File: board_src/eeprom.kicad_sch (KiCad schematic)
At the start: 5 parts, among them IC2 M24C02-WMN6TP, J6 Conn_01x02_Pin, J8 Conn_01x01_Pin

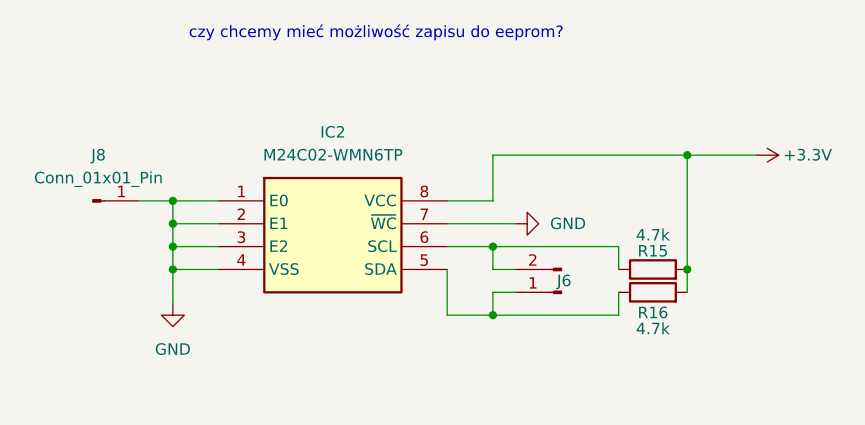
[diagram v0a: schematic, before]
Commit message: Wersja ze sciezkami miedzianymi
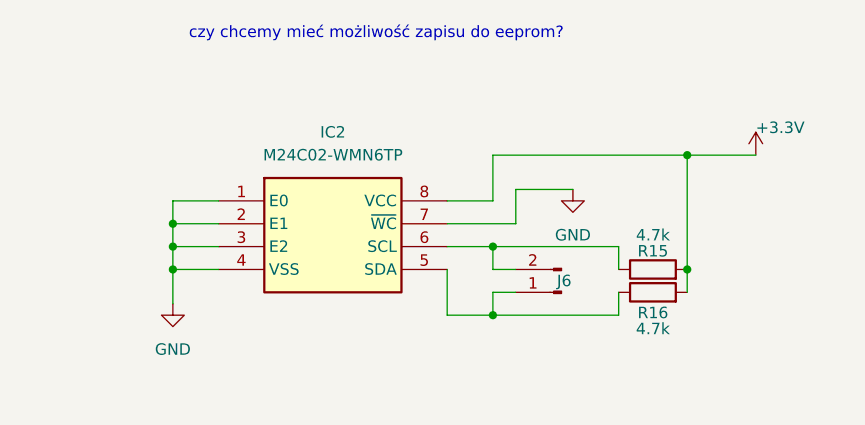
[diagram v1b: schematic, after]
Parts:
- removed J8: Conn_01x01_Pin, Connector_PinHeader_2.54mm:PinHeader_1x01_P2.54mm_Vertical, symbol Connector:Conn_01x01_Pin
- R15, R16: footprint Resistor_SMD:R_1206_3216Metric -> Resistor_SMD:R_0603_1608Metric
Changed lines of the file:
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@@
-	)
-	(junction
-		(at 149.86 90.17)
-		(diameter 0)
-		(color 0 0 0 0)
 	)
 	(junction
@@
 	(wire
 		(pts
-			(xy 146.05 90.17) (xy 149.86 90.17)
+			(xy 187.96 92.71) (xy 180.34 92.71)
 		)
 		(stroke
@@
 	(wire
 		(pts
-			(xy 180.34 92.71) (xy 187.96 92.71)
+			(xy 187.96 88.9) (xy 194.31 88.9)
 		)
 		(stroke
@@
 	(wire
 		(pts
+			(xy 187.96 88.9) (xy 187.96 92.71)
+		)
+		(stroke
+			(width 0)
+			(type default)
+		)
+	)
+	(wire
+		(pts
 			(xy 149.86 90.17) (xy 149.86 92.71)
 		)
@@
 			(width 0)
 			(type default)
-		)
-	)
-	(symbol
-		(lib_id "Connector:Conn_01x01_Pin")
-		(at 140.97 90.17 0)
-		(unit 1)
-		(exclude_from_sim no)
-		(in_bom yes)
-		(on_board yes)
-		(dnp no)
-		(fields_autoplaced yes)
-		(property "Reference" "J8"
-			(at 141.605 85.09 0)
-			(effects
-				(font
-					(size 1.27 1.27)
-				)
-			)
-		)
-		(property "Value" "Conn_01x01_Pin"
-			(at 141.605 87.63 0)
-			(effects
-				(font
-					(size 1.27 1.27)
-				)
-			)
-		)
-		(property "Footprint" "Connector_PinHeader_2.54mm:PinHeader_1x01_P2.54mm_Vertical"
-			(at 140.97 90.17 0)
-			(effects
-				(font
-					(size 1.27 1.27)
-				)
-				(hide yes)
-			)
-		)
-		(property "Datasheet" "~"
-			(at 140.97 90.17 0)
-			(effects
-				(font
-					(size 1.27 1.27)
-				)
-				(hide yes)
-			)
-		)
-		(property "Description" "Generic connector, single row, 01x01, script generated"
-			(at 140.97 90.17 0)
-			(effects
-				(font
-					(size 1.27 1.27)
-				)
-				(hide yes)
-			)
-		)
-		(pin "1"
-		)
-		(instances
-			(project ""
-				(path "/772e9f49-cfcf-4cf6-843d-0684684f2d4b/8b8e205f-8cd6-4f90-881c-a100662c7649"
-					(reference "J8")
-					(unit 1)
-				)
-			)
 		)
 	)
@@
 			)
 		)
-		(property "Footprint" "Resistor_SMD:R_1206_3216Metric"
+		(property "Footprint" "Resistor_SMD:R_0603_1608Metric"
 			(at 203.2 99.568 90)
 			(effects
@@
 	(symbol
 		(lib_id "power:+3.3V")
-		(at 214.63 85.09 270)
+		(at 214.63 85.09 0)
 		(unit 1)
 		(exclude_from_sim no)
@@
 		(dnp no)
 		(property "Reference" "#PWR010"
-			(at 210.82 85.09 0)
+			(at 214.63 88.9 0)
 			(effects
 				(font
@@
 		)
 		(property "Value" "+3.3V"
-			(at 217.678 85.09 90)
+			(at 214.63 82.042 0)
 			(effects
 				(font
@@
 	(symbol
 		(lib_id "power:GND")
-		(at 187.96 92.71 90)
+		(at 194.31 88.9 0)
 		(unit 1)
 		(exclude_from_sim no)
@@
 		(fields_autoplaced yes)
 		(property "Reference" "#PWR039"
-			(at 194.31 92.71 0)
+			(at 194.31 95.25 0)
 			(effects
 				(font
@@
 		)
 		(property "Value" "GND"
-			(at 191.77 92.7099 90)
-			(effects
-				(font
-					(size 1.27 1.27)
-				)
-				(justify right)
+			(at 194.31 93.98 0)
+			(effects
+				(font
+					(size 1.27 1.27)
+				)
 			)
 		)
 		(property "Footprint" ""
-			(at 187.96 92.71 0)
+			(at 194.31 88.9 0)
 			(effects
 				(font
@@
 		)
 		(property "Datasheet" ""
-			(at 187.96 92.71 0)
+			(at 194.31 88.9 0)
 			(effects
 				(font
@@
 		)
 		(property "Description" "Power symbol creates a global label with name \"GND\" , ground"
-			(at 187.96 92.71 0)
+			(at 194.31 88.9 0)
 			(effects
 				(font
@@
 			)
 		)
-		(property "Footprint" "Resistor_SMD:R_1206_3216Metric"
+		(property "Footprint" "Resistor_SMD:R_0603_1608Metric"
 			(at 203.2 102.108 90)
 			(effects

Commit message: sciezki polaczen
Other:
- note removed: "czy chcemy mieć możliwość zapisu do eeprom?"
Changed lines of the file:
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@@
 	(generator_version "9.0")
 	(paper "A4")
-	(text "czy chcemy mieć możliwość zapisu do eeprom?"
-		(exclude_from_sim no)
-		(at 172.466 71.628 0)
-		(effects
-			(font
-				(size 1.27 1.27)
-			)
-		)
-	)
 	(junction
 		(at 149.86 97.79)

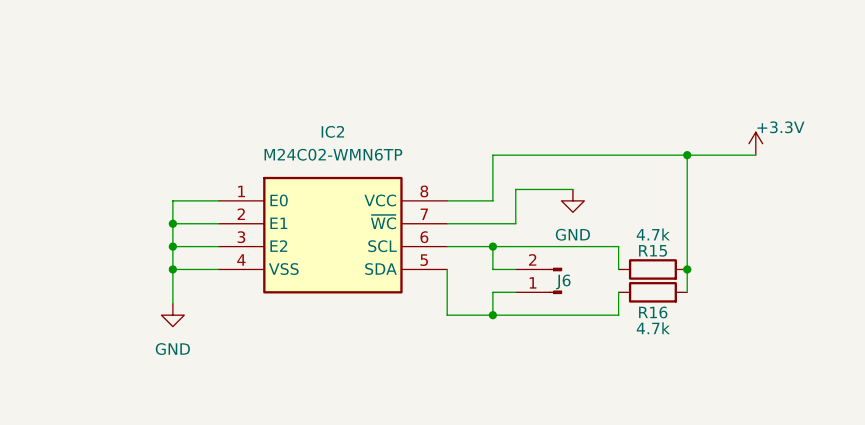
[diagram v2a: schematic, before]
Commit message: poprawione polaczenia diod i wartosci opornikow, aktualizacja niektorych elementow ze wzgledu na braki w magazynie
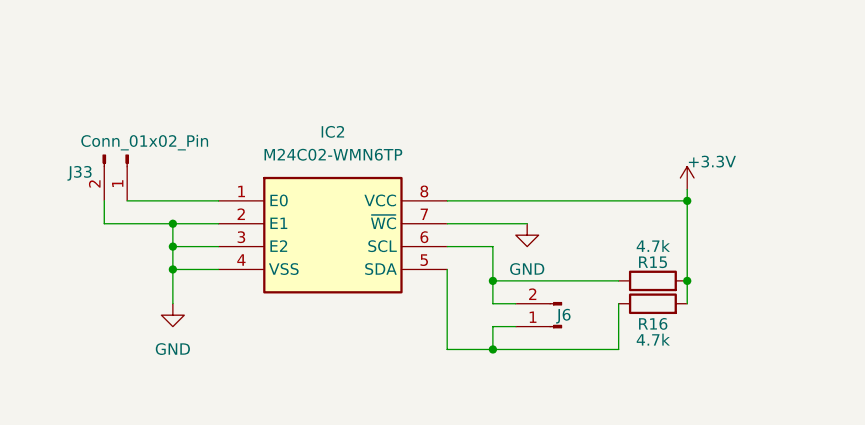
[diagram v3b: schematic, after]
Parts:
- added J33: Conn_01x02_Pin, Connector_PinHeader_2.54mm:PinHeader_1x02_P2.54mm_Vertical, symbol Connector:Conn_01x02_Pin
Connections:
- net GND: now also J33.2 (Pin_2); no longer IC2.1 (E0)
- new net: IC2.1 (E0), J33.1 (Pin_1)
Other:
- moved on the sheet: J6, R15, R16

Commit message: Poprawki w schematach. Rozpoczęte korekty płytki
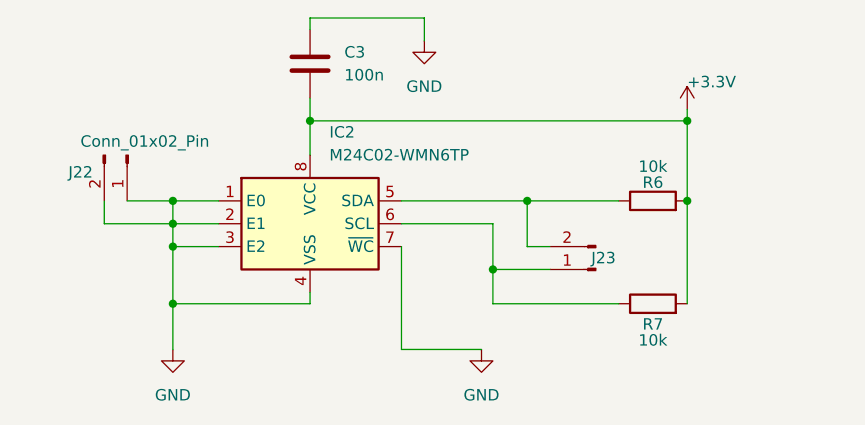
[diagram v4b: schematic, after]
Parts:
- added C3: 100n, Capacitor_SMD:C_0603_1608Metric_Pad1.08x0.95mm_HandSolder, symbol Device:C
- IC2: footprint footprints:EEPROM -> Package_SO:SOIC-8_3.9x4.9mm_P1.27mm; symbol M24C02-WMN6TP:M24C02-WMN6TP -> Memory_EEPROM:M24C02-WMN
- J22: renamed from J33; footprint Connector_PinHeader_2.54mm:PinHeader_1x02_P2.54mm_Vertical -> Connector_PinHeader_2.54mm:PinHeader_2x20_P2.54mm_Vertical
- J23: renamed from J6; footprint Connector_PinHeader_2.54mm:PinHeader_1x02_P2.54mm_Vertical -> Connector_PinHeader_2.54mm:PinHeader_1x04_P2.54mm_Vertical
- R6: renamed from R15; value 4.7k -> 10k; footprint Resistor_SMD:R_0603_1608Metric -> Resistor_SMD:R_0603_1608Metric_Pad0.98x0.95mm_HandSolder
- R7: renamed from R16; value 4.7k -> 10k; footprint Resistor_SMD:R_0603_1608Metric -> Resistor_SMD:R_0603_1608Metric_Pad0.98x0.95mm_HandSolder
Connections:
- net +3.3V: now also C3.1
- net GND: now also IC2.1 (E0), J22.1 (Pin_1), C3.2
- net at J23.2 (Pin_2), R6.1: now also IC2.5 (SDA); no longer IC2.6 (SCL)
- net at J23.1 (Pin_1), R7.1: now also IC2.6 (SCL); no longer IC2.5 (SDA)
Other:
- moved on the sheet: IC2, J23, R6

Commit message: Naniesione poprawki na projekcie płytki. Wersja końcowa
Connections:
- net at IC2.5 (SDA), R6.1: now also J23.1 (Pin_1); no longer J23.2 (Pin_2)
- net at IC2.6 (SCL), R7.1: now also J23.2 (Pin_2); no longer J23.1 (Pin_1)
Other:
- moved on the sheet: J23
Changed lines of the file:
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@@
 	(symbol
 		(lib_id "Connector:Conn_01x02_Pin")
-		(at 196.85 97.79 180)
+		(at 196.85 95.25 0)
+		(mirror y)
 		(unit 1)
 		(exclude_from_sim no)
@@
 		)
 		(property "Value" "Conn_01x02_Pin"
-			(at 200.914 94.996 0)
+			(at 200.914 98.044 0)
 			(effects
 				(font
@@
 		)
 		(property "Footprint" "Connector_PinHeader_2.54mm:PinHeader_1x04_P2.54mm_Vertical"
-			(at 196.85 97.79 0)
+			(at 196.85 95.25 0)
 			(effects
 				(font
@@
 		)
 		(property "Datasheet" "~"
-			(at 196.85 97.79 0)
+			(at 196.85 95.25 0)
 			(effects
 				(font
@@
 		)
 		(property "Description" "Generic connector, single row, 01x02, script generated"
-			(at 196.85 97.79 0)
+			(at 196.85 95.25 0)
 			(effects
 				(font

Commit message: Wprowadzono usprawnienia i poprawki. Wersja ostateczna, wysłana do JLCPCB.
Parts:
- J22: footprint Connector_PinHeader_2.54mm:PinHeader_2x20_P2.54mm_Vertical -> Connector_PinHeader_2.54mm:PinHeader_1x02_P2.54mm_Vertical
- J23: footprint Connector_PinHeader_2.54mm:PinHeader_1x04_P2.54mm_Vertical -> Connector_PinHeader_2.54mm:PinHeader_1x02_P2.54mm_Vertical
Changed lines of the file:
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@@
 			)
 		)
-		(property "Footprint" "Connector_PinHeader_2.54mm:PinHeader_1x04_P2.54mm_Vertical"
+		(property "Footprint" "Connector_PinHeader_2.54mm:PinHeader_1x02_P2.54mm_Vertical"
 			(at 196.85 95.25 0)
 			(effects
@@
 			)
 		)
-		(property "Footprint" "Connector_PinHeader_2.54mm:PinHeader_2x20_P2.54mm_Vertical"
+		(property "Footprint" "Connector_PinHeader_2.54mm:PinHeader_1x02_P2.54mm_Vertical"
 			(at 144.78 85.09 0)
 			(effects
